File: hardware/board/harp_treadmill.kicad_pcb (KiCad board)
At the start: 4 copper layers, 80 x 100 mm, 163 parts, among them J1 Conn_01x03_Male, J2 AudioJack3, J3 Conn_01x05_Female, J4 Conn_01x02_Female, J5 USB_C_Receptacle_USB2.0, J6 Barrel_Jack_Switch, J7 Conn_01x04_Female, Q2 Si7336ADP, U1 LP2985-3.3, U10 AD8615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

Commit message: add comment about race condition
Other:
- board text added: "Jan 5, 2024"
- board text removed: "Jan 5, 2023"
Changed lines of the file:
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@@
       (drillshape 0)
       (scaleselection 1)
-      (outputdirectory "exports/harp_treadmill_v0.1.0/gerbers/")
+      (outputdirectory "exports/harp_treadmill_v0.2.0/gerbers/")
     )
   )
@@
     (effects (font (size 1.25 1.25) (thickness 0.2) bold) (justify left bottom))
   )
-  (gr_text "Jan 5, 2023" (at 107.5 126.5) (layer "F.SilkS")
+  (gr_text "Jan 5, 2024" (at 107.5 126.5) (layer "F.SilkS")
     (effects (font (size 0.7 0.7) (thickness 0.1)) (justify left bottom))
   )

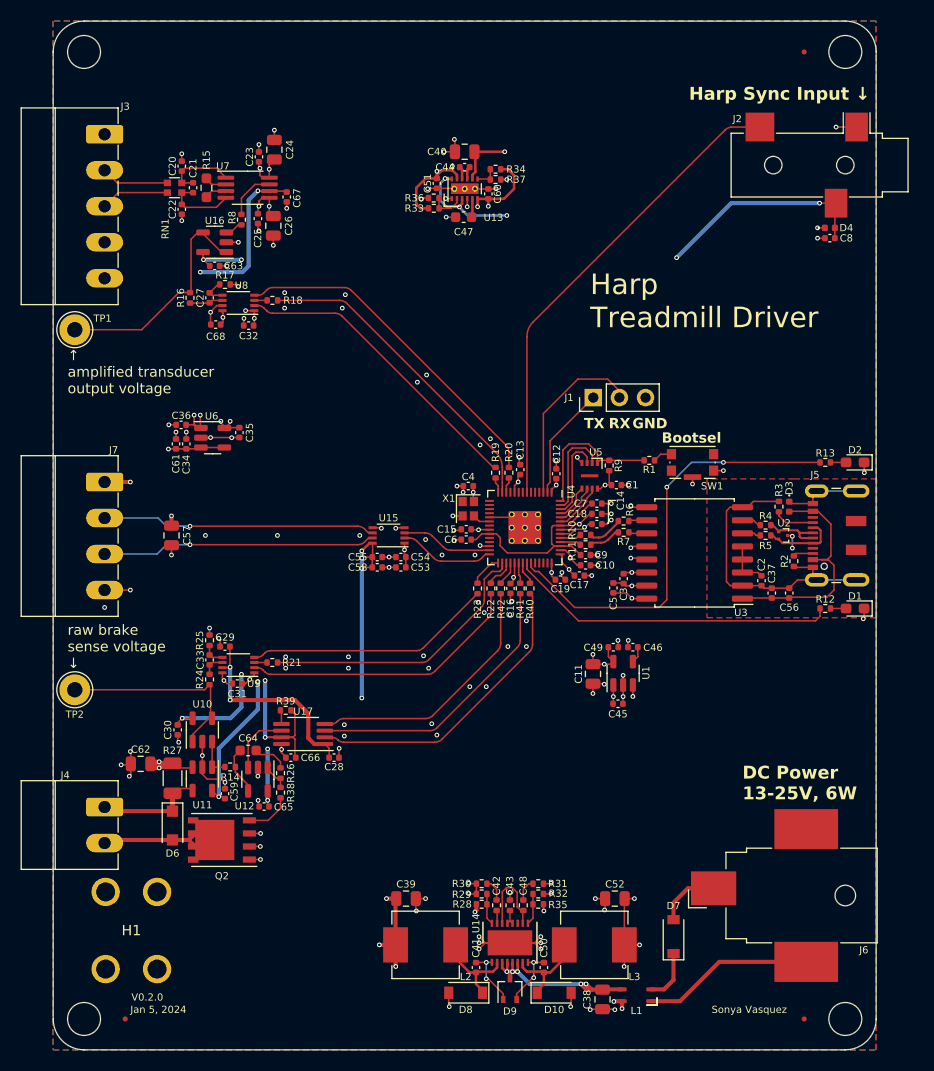
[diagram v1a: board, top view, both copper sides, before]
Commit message: update silkscreen size; add mating connector note
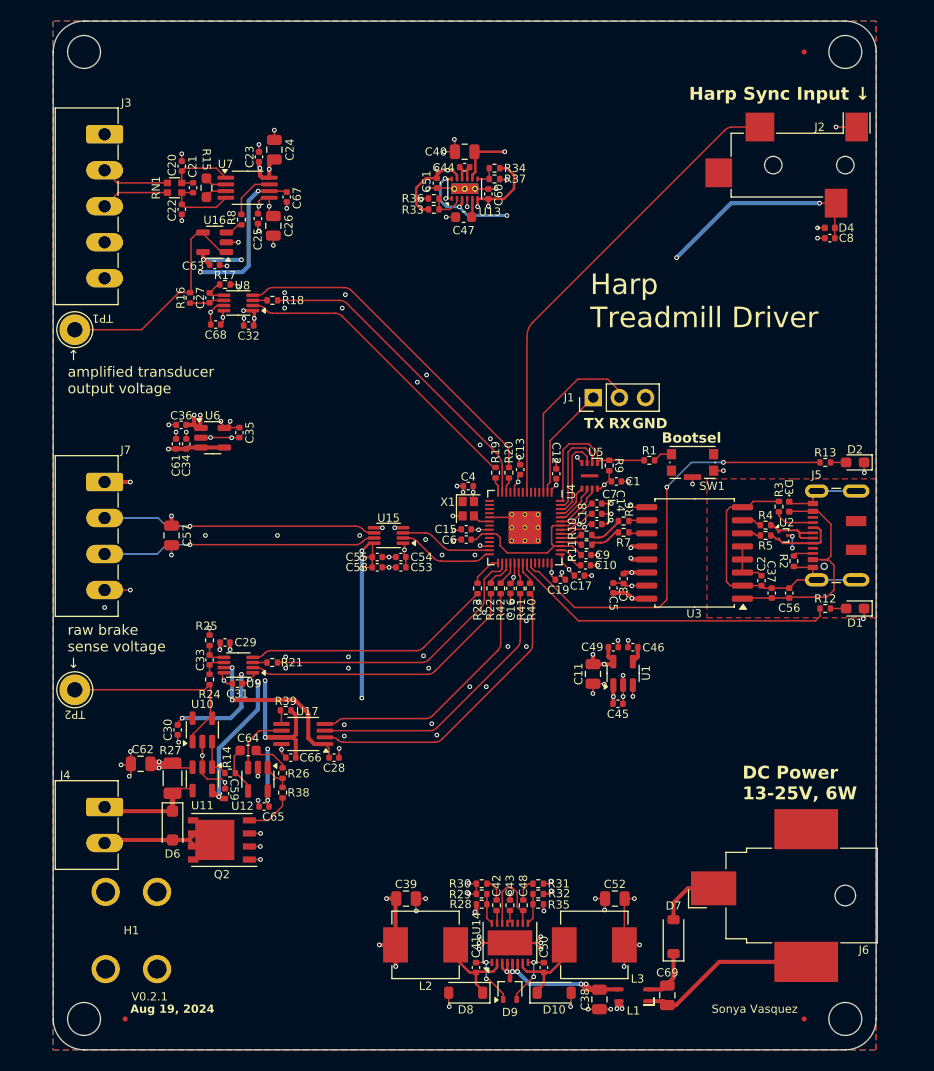
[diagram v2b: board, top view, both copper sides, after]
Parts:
- added C69: 10uF, Capacitor_SMD:C_0805_2012Metric, F.Cu at (159.7, 124.7)
- J2: footprint Connector_Audio:Jack_3.5mm_CUI_SJ-3523-SMT_Horizontal -> Connector_Audio:Jack_3.5mm_CUI_SJ-3524-SMT_Horizontal
- moved R14 0.60 mm to (117.2, 103.1)
- moved C29 0.40 mm to (116.7, 90.4)
- moved C1 0.35 mm to (154.8, 74.8)
- moved C38 0.30 mm to (153.1, 125.1)
- moved L1 0.30 mm to (156.4, 124.7)
- moved R26 0.20 mm to (122.3, 103.1)
- moved R38 0.20 mm to (122.3, 105.0)
- moved R34 0.14 mm to (142.9, 44.3)
- moved R37 0.11 mm to (142.9, 45.4)
- moved C63 0.10 mm to (115.7, 53.7)
- moved R10 0.10 mm to (151.8, 80.0)
- moved R11 0.10 mm to (151.8, 80.9)
- moved R33 0.10 mm to (137.0, 48.3)
- moved C9 0.05 mm to (151.8, 81.9)
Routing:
- net VREF_3V3: track 25.7 -> 24.3 mm, vias 5 -> 6
- net GND2: track 16.7 -> 17.3 mm
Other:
- board text added: "Aug 19, 2024"
- board text added: "V0.2.1"
- board text removed: "Jan 5, 2024"
- board text removed: "V0.2.0"
